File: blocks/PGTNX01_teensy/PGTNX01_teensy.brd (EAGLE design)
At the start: 69.9 x 53.3 mm, 89 parts, among them IC1 7805L

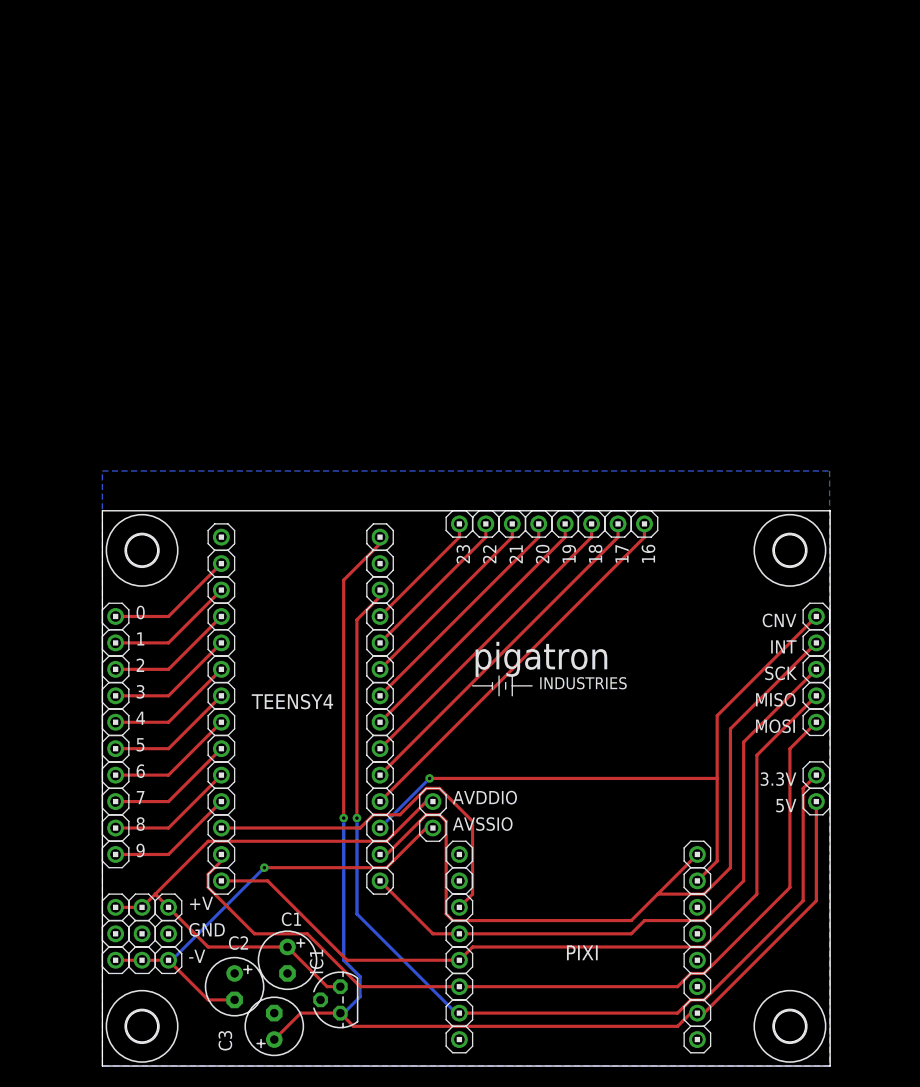
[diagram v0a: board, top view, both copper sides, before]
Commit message: Modified boards to fit together better
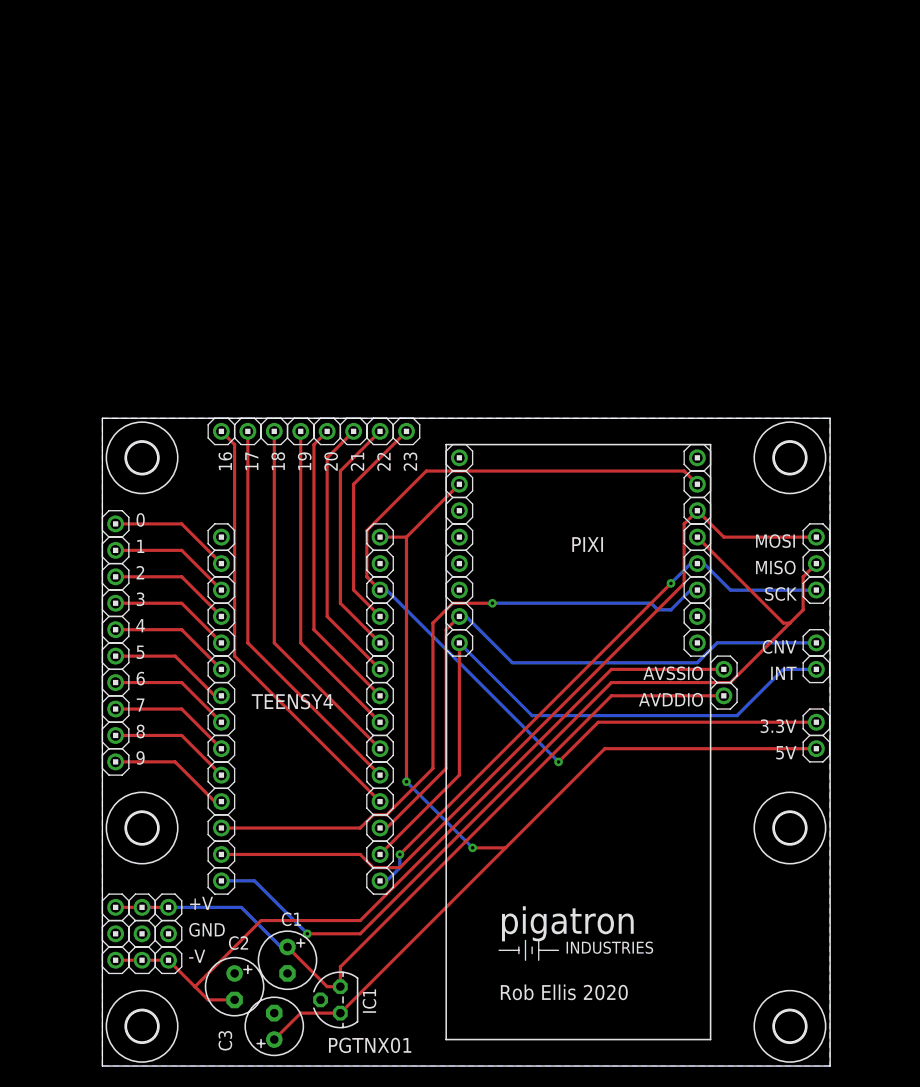
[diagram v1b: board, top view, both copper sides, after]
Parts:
- added U$6, U$7: (no value), mechanical:STANDOFF/3.0
- moved PIXI_GND 60.4 mm to (57.1, 58.4), turned to 180 degrees
- moved PIXI_GND2 60.4 mm to (34.3, 58.4), turned to 0 degrees
- moved PIXI_3.3V 55.7 mm to (57.1, 55.9), turned to 180 degrees
- moved PIXI_5V 55.7 mm to (34.3, 55.9), turned to 0 degrees
- moved U$2 54.6 mm to (3.81, 58.4)
- moved PIXI_NC6 51.1 mm to (34.3, 53.3), turned to 0 degrees
- moved PIXI_SDI 51.1 mm to (57.1, 53.3), turned to 180 degrees
- moved PIXI_NC5 46.6 mm to (34.3, 50.8), turned to 0 degrees
- moved PIXI_SDO 46.6 mm to (57.1, 50.8), turned to 180 degrees
- moved PIXI_NC4 42.3 mm to (34.3, 48.3), turned to 0 degrees
- moved PIXI_SCK 42.3 mm to (57.1, 48.3), turned to 180 degrees
- moved 16 41.6 mm to (11.4, 61.0)
- moved PIXI_CS 38.1 mm to (57.1, 45.7), turned to 180 degrees
- moved PIXI_NC3 38.1 mm to (34.3, 45.7), turned to 0 degrees
- moved 17 36.7 mm to (14.0, 61.0)
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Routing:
- net -12V: track 43.7 -> 76.4 mm, vias 1 -> 0
- net N$8: track 35.8 -> 63.9 mm, vias 0 -> 1
- net +12V: track 56.2 -> 74.3 mm
- net N$9: track 77.2 -> 62.5 mm
- net N$6: track 78.6 -> 88.2 mm, vias 0 -> 1
- net N$16: track 12.0 -> 20.9 mm
- net N$5: track 84.4 -> 76.3 mm
- net N$1: track 117.0 -> 109.0 mm, vias 1 -> 2
- net N$15: track 15.6 -> 23.5 mm
- net N$14: track 19.2 -> 26.0 mm
- net N$7: track 62.3 -> 56.3 mm, vias 0 -> 2
- net N$13: track 22.8 -> 28.6 mm
- net N$3: track 95.9 -> 91.2 mm
- net N$4: track 37.2 -> 41.9 mm
- net N$2: track 33.6 -> 38.3 mm
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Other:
- board size 69.9 x 53.3 mm -> 69.9 x 62.2 mm
- board text added: "PGTNX01"
- board text added: "Rob Ellis 2020"

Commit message: Added output resistors and xener voltage limiters.
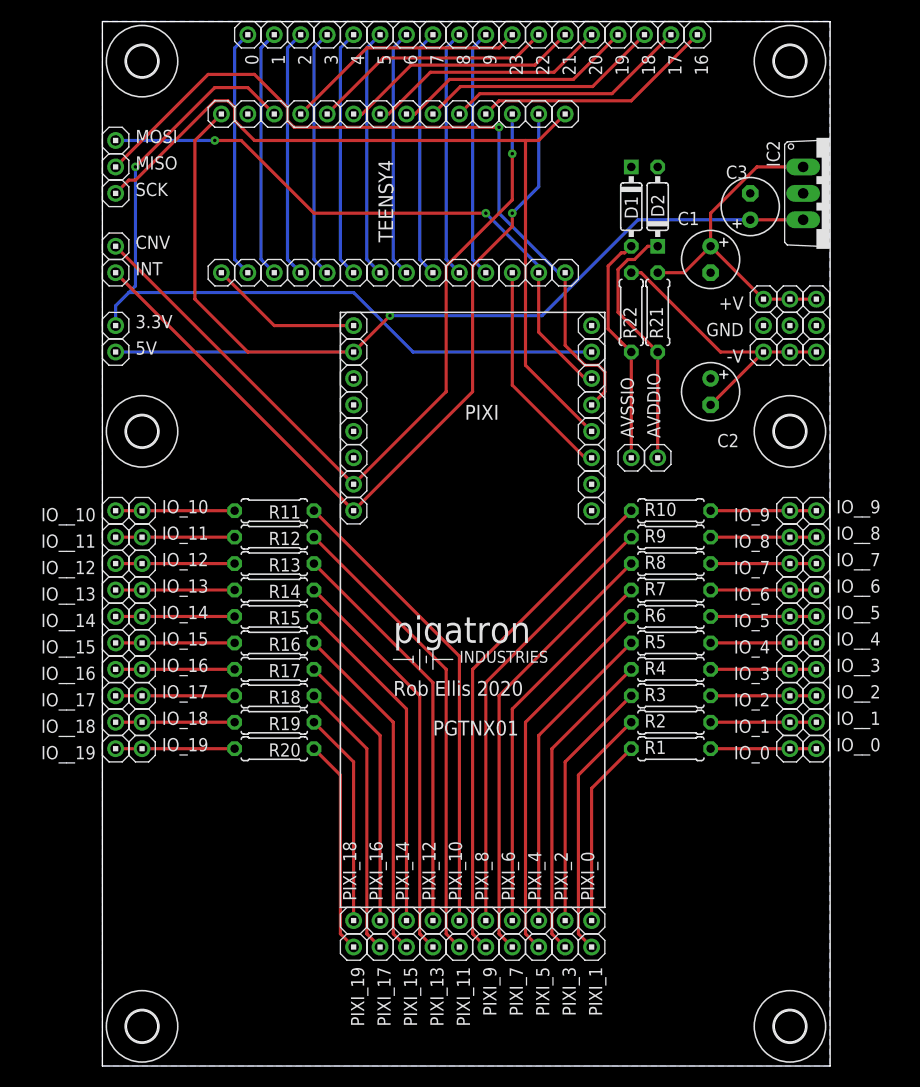
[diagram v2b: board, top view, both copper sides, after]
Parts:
- removed IC1: 7805L, ic_voltage_reg:TO92
- added D1, D2: (no value), transistors:DO35-7
- added IC2: 7805TV, ic_voltage_reg:TO220V
- added IO_0, IO_1, IO_10, IO_11, IO_12, IO_13, IO_14, IO_15, IO_16, IO_17, IO_18, IO_19, IO_2, IO_3, IO_4, IO_5, IO_6, IO_7, IO_8, IO_9, IO__0, IO__1, IO__10, IO__11, IO__12, IO__13, IO__14, IO__15, IO__16, IO__17, IO__18, IO__19, IO__2, IO__3, IO__4, IO__5, IO__6, IO__7, IO__8, IO__9, PIXI_0, PIXI_1, PIXI_10, PIXI_11, PIXI_12, PIXI_13, PIXI_14, PIXI_15, PIXI_16, PIXI_17, PIXI_18, PIXI_19, PIXI_2, PIXI_3, PIXI_4, PIXI_5, PIXI_6, PIXI_7, PIXI_8, PIXI_9: HEADER/MALE/01, connectors:HEADER/MALE/01
- added R1, R10, R11, R12, R13, R14, R15, R16, R17, R18, R19, R2, R20, R21, R22, R3, R4, R5, R6, R7, R8, R9: (no value), resistors:RESISTOR/7.5
- C3: value 1uF -> 0.1uF
- moved C3 91.1 mm to (62.2, 82.5)
- moved +V3 89.1 mm to (68.6, 73.7)
- moved -V3 89.1 mm to (68.6, 68.6)
- moved GND2 89.1 mm to (68.6, 71.1)
- moved -V2 85.4 mm to (66.0, 68.6)
- moved GND3 85.4 mm to (66.0, 71.1)
- moved +V2 85.4 mm to (66.0, 73.7)
- moved +V 81.7 mm to (63.5, 73.7), turned to 180 degrees
- moved -V 81.7 mm to (63.5, 68.6), turned to 180 degrees
- moved GND 81.7 mm to (63.5, 71.1), turned to 180 degrees
- moved C1 78.6 mm to (58.4, 77.5)
- moved 9 78.4 mm to (36.8, 99.1), turned to 270 degrees
- moved 3.3V 77.3 mm to (1.27, 71.1), turned to 0 degrees
- moved INT 77.3 mm to (1.27, 76.2), turned to 0 degrees
- moved MISO 77.3 mm to (1.27, 86.4), turned to 0 degrees
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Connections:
- new net +5V: 5V.1, C3.+, IC2.3, PIXI_5V.1, TNSY_VIN.1
- new net N$27: IO_1.1, IO__1.1, R2.2
- new net N$29: IO_0.1, IO__0.1, R1.2
- new net N$3: PIXI_1.1, R2.1
- new net N$30: PIXI_2.1, R3.1
- new net N$31: IO_2.1, IO__2.1, R3.2
- new net N$32: PIXI_3.1, R4.1
- new net N$33: IO_3.1, IO__3.1, R4.2
- new net N$34: PIXI_4.1, R5.1
- new net N$35: IO_4.1, IO__4.1, R5.2
- new net N$36: PIXI_5.1, R6.1
- new net N$37: IO_5.1, IO__5.1, R6.2
- new net N$38: PIXI_6.1, R7.1
- new net N$39: IO_6.1, IO__6.1, R7.2
- new net N$40: PIXI_7.1, R8.1
- new net N$41: IO_7.1, IO__7.1, R8.2
- new net N$42: PIXI_8.1, R9.1
- new net N$43: IO_8.1, IO__8.1, R9.2
- new net N$44: PIXI_9.1, R10.1
- new net N$45: IO_9.1, IO__9.1, R10.2
- new net N$46: PIXI_10.1, R11.1
- new net N$47: IO_10.1, IO__10.1, R11.2
- new net N$48: PIXI_11.1, R12.1
- new net N$49: IO_11.1, IO__11.1, R12.2
- new net N$50: PIXI_12.1, R13.1
- new net N$51: IO_12.1, IO__12.1, R13.2
- new net N$52: PIXI_13.1, R14.1
- new net N$53: IO_13.1, IO__13.1, R14.2
- new net N$54: PIXI_14.1, R15.1
- new net N$55: IO_14.1, IO__14.1, R15.2
- new net N$56: PIXI_15.1, R16.1
- new net N$57: IO_15.1, IO__15.1, R16.2
- new net N$58: PIXI_16.1, R17.1
- new net N$59: IO_16.1, IO__16.1, R17.2
- new net N$60: PIXI_17.1, R18.1
- new net N$61: IO_17.1, IO__17.1, R18.2
- new net N$62: PIXI_18.1, R19.1
- new net N$63: IO_18.1, IO__18.1, R19.2
- new net N$64: PIXI_19.1, R20.1
- new net N$65: IO_19.1, IO__19.1, R20.2
- new net N$66: AVDDIO.1, D2.C, R21.1
- new net N$67: AVSSIO.1, D1.A, R22.1
- net +12V: now also IC2.1, R21.2; no longer AVDDIO.1, IC1.3
- net -12V: now also R22.2; no longer AVSSIO.1
- net GND: now also D1.C, D2.A, IC2.2; no longer IC1.2
- net N$1: now also PIXI_0.1, R1.1; no longer 5V.1, C3.+, IC1.1, PIXI_5V.1, TNSY_VIN.1
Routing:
- net +5V: track 0.00 -> 107.5 mm, vias 0 -> 1
- net N$1: track 109.0 -> 18.1 mm, vias 2 -> 0
- net N$44: track 0.00 -> 48.7 mm
- net -12V: track 76.4 -> 28.1 mm
- net N$48: track 0.00 -> 45.2 mm
- net N$46: track 0.00 -> 45.2 mm
- net N$42: track 0.00 -> 42.6 mm
- net N$40: track 0.00 -> 42.6 mm
- net N$8: track 63.9 -> 21.3 mm, vias 1 -> 0
- net +12V: track 74.3 -> 32.3 mm
- net N$52: track 0.00 -> 39.0 mm
- net N$50: track 0.00 -> 39.0 mm
- net N$38: track 0.00 -> 36.5 mm
- net N$36: track 0.00 -> 36.5 mm
- net N$56: track 0.00 -> 32.9 mm
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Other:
- board size 69.9 x 62.2 mm -> 69.9 x 100.3 mm

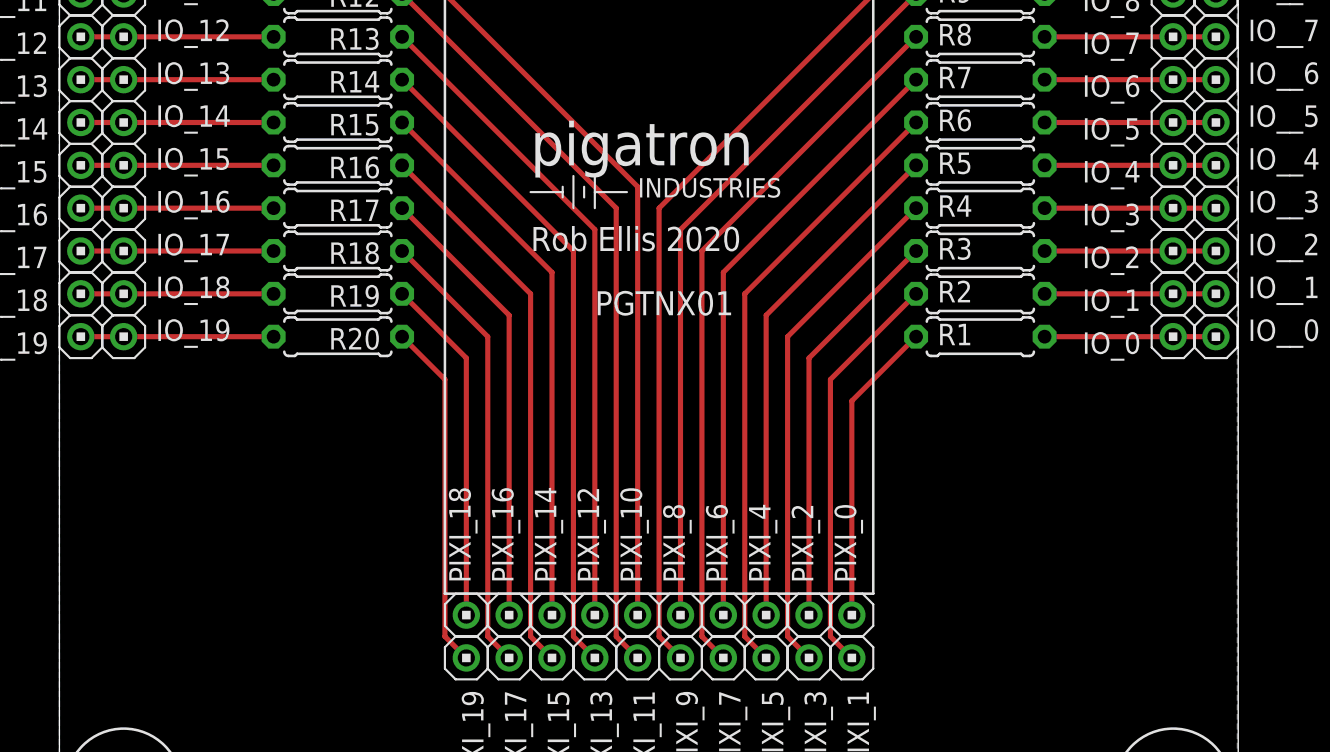
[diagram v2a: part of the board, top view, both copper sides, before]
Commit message: new design pcbs for midi2cv
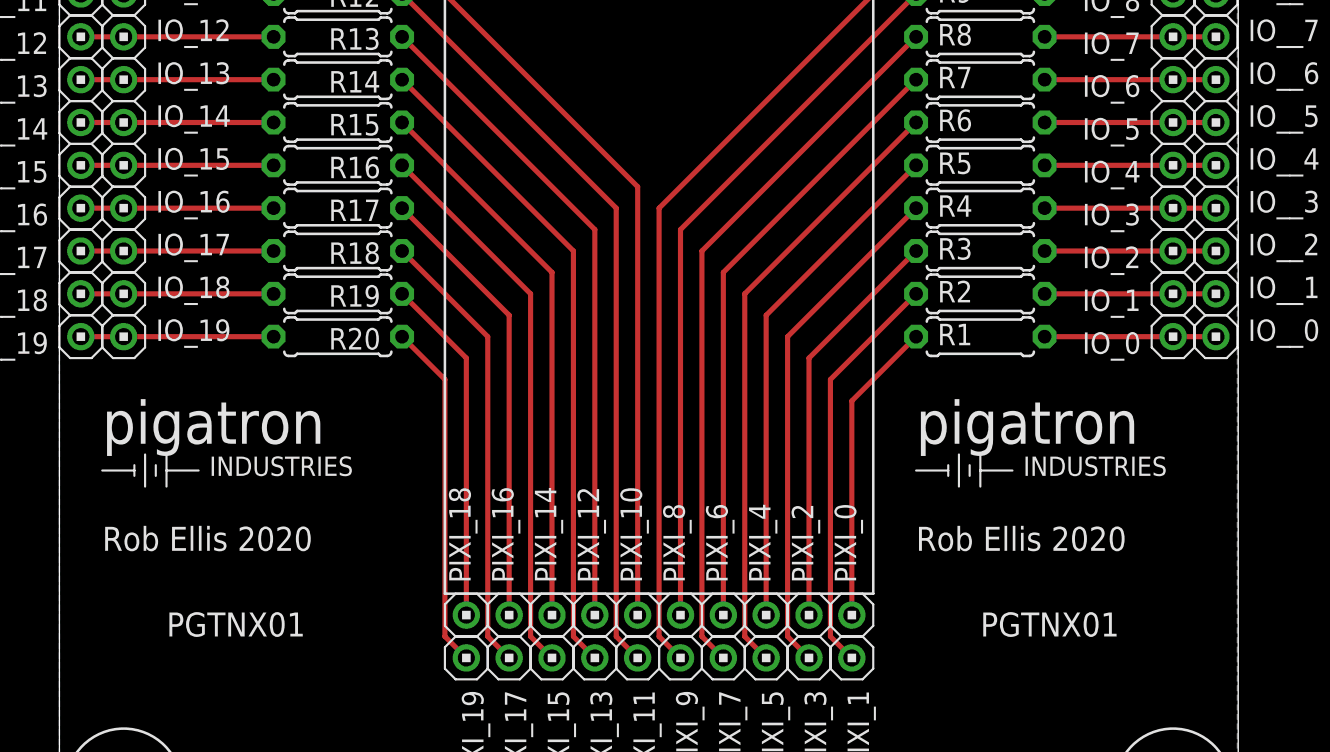
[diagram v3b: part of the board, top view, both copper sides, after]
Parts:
- added U$8: (no value), mechanical:PIGATRON-LOGO
- moved U$5 30.3 mm to (11.4, 24.1)
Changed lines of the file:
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@@
 <wire x1="22.86" y1="72.39" x2="48.26" y2="72.39" width="0.1524" layer="21"/>
 <wire x1="48.26" y1="72.39" x2="48.26" y2="15.24" width="0.1524" layer="21"/>
-<text x="27.94" y="35.56" size="1.4224" layer="25" ratio="10">Rob Ellis 2020</text>
+<text x="2.54" y="17.78" size="1.4224" layer="25" ratio="10">Rob Ellis 2020</text>
 <dimension x1="3.81" y1="96.52" x2="3.81" y2="60.96" x3="-5.08" y3="78.74" textsize="1.778" layer="48"/>
-<text x="31.75" y="31.75" size="1.4224" layer="25" ratio="10">PGTNX01</text>
+<text x="6.35" y="12.7" size="1.4224" layer="25" ratio="10">PGTNX01</text>
 <dimension x1="78.74" y1="0" x2="78.74" y2="100.33" x3="85.09" y3="50.165" textsize="1.778" layer="48"/>
+<dimension x1="68.58" y1="68.58" x2="68.58" y2="60.96" x3="78.74" y3="64.77" textsize="1.778" layer="51"/>
+<dimension x1="68.58" y1="53.34" x2="68.58" y2="60.96" x3="78.74" y3="57.15" textsize="1.778" layer="51"/>
+<text x="50.8" y="17.78" size="1.4224" layer="25" ratio="10">Rob Ellis 2020</text>
+<text x="54.61" y="12.7" size="1.4224" layer="25" ratio="10">PGTNX01</text>
 </plain>
 <attributes>
@@
 <attribute name="SPICEPREFIX" value="X" x="1.27" y="71.12" size="1.778" layer="27" display="off"/>
 </element>
-<element name="U$5" library="mechanical" package="PIGATRON-LOGO" value="" x="36.83" y="40.64"/>
+<element name="U$5" library="mechanical" package="PIGATRON-LOGO" value="" x="11.43" y="24.13"/>
 <element name="U$6" library="mechanical" package="STANDOFF/3.0" value="" x="66.04" y="60.96"/>
 <element name="U$4" library="mechanical" package="STANDOFF/3.0" value="" x="66.04" y="3.81"/>
@@
 <element name="D1" library="transistors" package="DO35-7" value="" x="50.8" y="82.55" rot="R270"/>
 <element name="D2" library="transistors" package="DO35-7" value="" x="53.34" y="82.55" rot="R90"/>
+<element name="U$8" library="mechanical" package="PIGATRON-LOGO" value="" x="59.69" y="24.13"/>
 </elements>
 <signals>

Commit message: Added correct diode type BZX55C12
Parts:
- D1, D2: value (none) -> BZX55C12
